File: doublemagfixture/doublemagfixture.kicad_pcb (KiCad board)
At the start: 2 copper layers, 106.7 x 64.1 mm, 29 parts, among them J1 Barrel_Jack_MountingPin, J2 Screw_Terminal_01x04, J3 Screw_Terminal_01x04, J4 Screw_Terminal_01x04, J5 Screw_Terminal_01x04, J6 Screw_Terminal_01x08, J7 Screw_Terminal_01x08, U1 easydriver_stepper_driver, U2 easydriver_stepper_driver, U3 easydriver_stepper_driver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

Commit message: almost done pcb
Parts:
- added H1: MountingHole, MountingHole:MountingHole_3.2mm_M3_Pad, F.Cu at (8.89, 14.0)
- added H2: MountingHole, MountingHole:MountingHole_3.2mm_M3_Pad, F.Cu at (5.08, 70.5)
- added H3: MountingHole, MountingHole:MountingHole_3.2mm_M3_Pad, F.Cu at (86.4, 70.5)
- D1: value DIR_IND -> DIR0
- D2: value DIR_IND -> DIR1
- D3: value STEP_IND -> STEP0
- D4: value STEP_IND -> STEP1
- D5: value DIR_IND -> DIR2
- D6: value DIR_IND -> DIR3
- D7: value STEP_IND -> STEP2
- D8: value STEP_IND -> STEP3
- moved J6 269.8 mm to (49.5, 6.35), turned to 0 degrees
- moved D8 258.6 mm to (68.6, 15.9)
- moved D6 257.5 mm to (62.2, 15.9)
- moved D7 252.2 mm to (54.6, 15.9)
- moved R7 251.7 mm to (71.8, 21.0)
- moved R8 251.7 mm to (76.8, 21.0)
- moved U4 251.7 mm to (74.3, 36.2)
- moved J5 251.3 mm to (66.7, 71.1)
- moved D5 251.1 mm to (48.3, 15.9)
- moved R6 251.1 mm to (55.9, 21.0)
- moved U3 251.1 mm to (53.3, 36.2)
- moved R5 251.1 mm to (50.8, 21.0)
- moved U2 250.6 mm to (32.4, 36.2)
- moved R3 250.6 mm to (29.8, 21.0)
- moved R4 250.6 mm to (34.9, 21.0)
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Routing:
- net /dir0: track 0.00 -> 62.6 mm
- net /dir1: track 0.00 -> 50.3 mm
- net /step0: track 0.00 -> 47.3 mm
- net +5V: track 0.00 -> 43.5 mm
- net /step1: track 0.00 -> 35.5 mm
- net /dir2: track 0.00 -> 32.1 mm
- net /dir3: track 0.00 -> 31.3 mm
- net /step3: track 0.00 -> 30.8 mm
- net /step2: track 0.00 -> 29.4 mm
- net Net-(J2-Pad4): track 0.00 -> 29.1 mm
- net +12V: track 71.1 -> 98.5 mm
- net /lim0: track 0.00 -> 25.2 mm
- net /lim1: track 0.00 -> 21.4 mm
- net Net-(D3-Pad2): track 0.00 -> 17.3 mm
- net Net-(D1-Pad2): track 0.00 -> 16.1 mm
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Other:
- board size 106.7 x 64.1 mm -> 90.2 x 74.3 mm
- board text added: "+12V"
- board text added: "+5V"
- board text added: "0"
- board text added: "1"
- board text added: "2"
- board text added: "3"
- board text added: "A+"
- board text added: "A-"
- board text added: "B+"
- board text added: "B-"
- board text added: "D0"
- board text added: "D1"
- board text added: "D2"
- board text added: "D3"
- board text added: "DIR"
- board text added: "GND"
- board text added: "L0"
- board text added: "L1"
- board text added: "NC"
- board text added: "S0"
- board text added: "S1"
- board text added: "S2"
- board text added: "S3"
- board text added: "STEP"

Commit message: Final(?) pcb
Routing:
- net GND: vias 0 -> 3

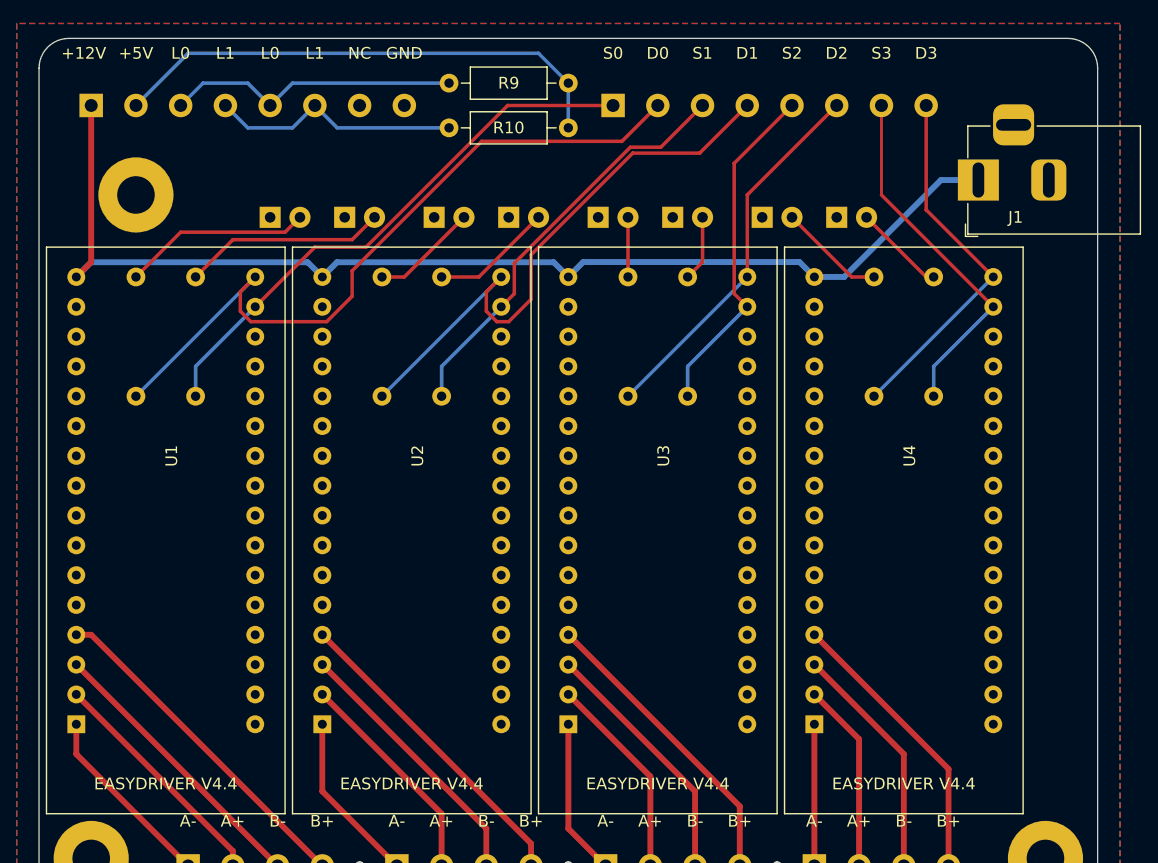
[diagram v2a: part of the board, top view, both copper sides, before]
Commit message: numbering fixes and wider traces on power line
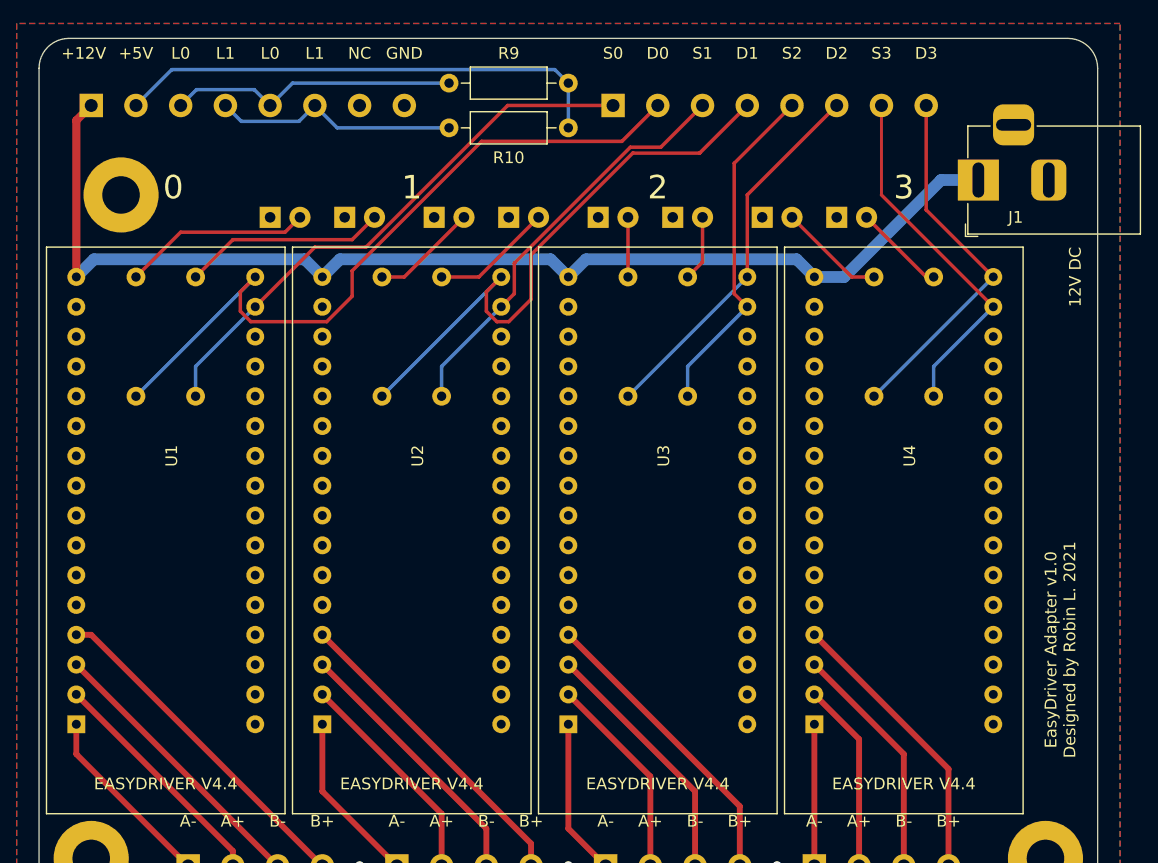
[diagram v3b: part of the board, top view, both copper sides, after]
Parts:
- moved H1 1.27 mm to (7.62, 14.0)
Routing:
- net +5V: track 43.5 -> 42.4 mm
- net +12V: track 98.5 -> 99.1 mm
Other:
- board text added: "12V DC"
- board text added: "EasyDriver Adapter v1.0 Designed by Robin L. 2021"
- board text added: "JLCJLCJLCJLC"

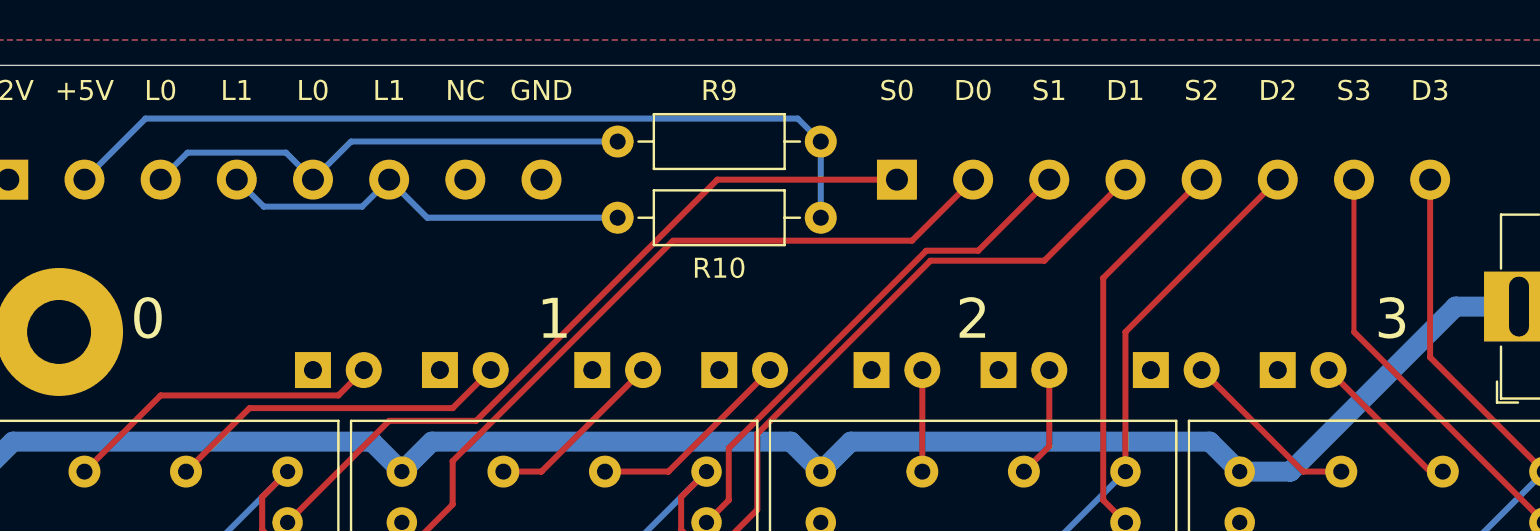
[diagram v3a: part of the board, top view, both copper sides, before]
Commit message: moved leds to front
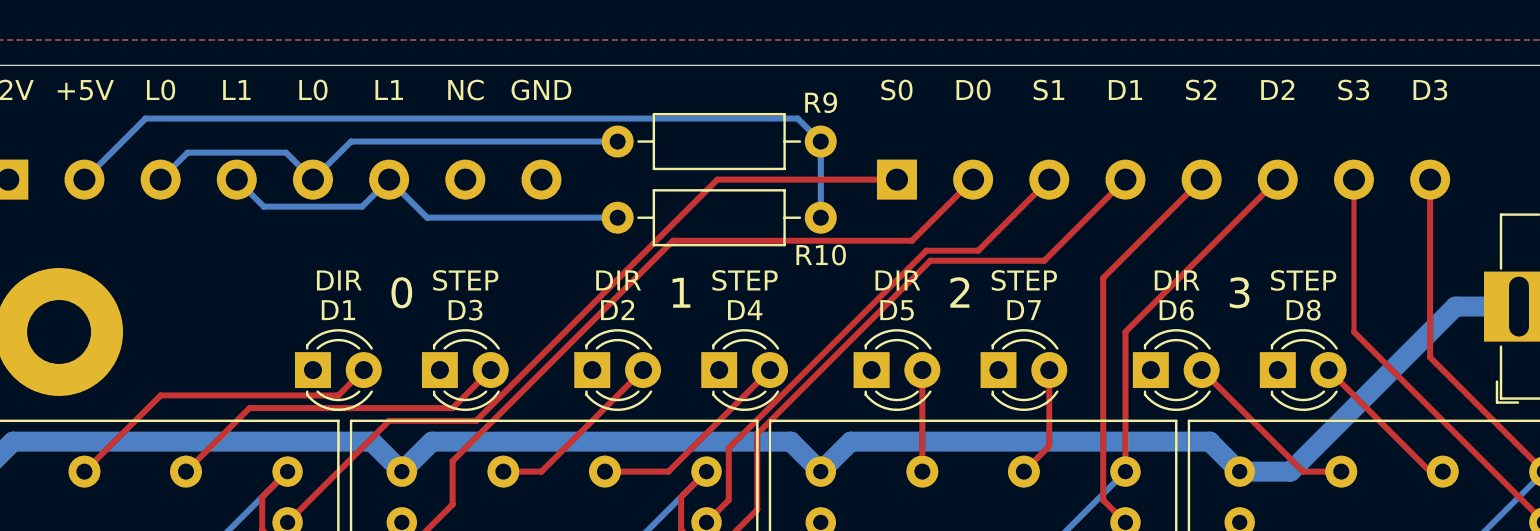
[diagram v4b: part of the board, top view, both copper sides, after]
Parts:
- D1, D2, D3, D4, D5, D6, D7, D8: moved to F.Cu
